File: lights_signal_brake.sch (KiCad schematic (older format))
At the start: 33 parts

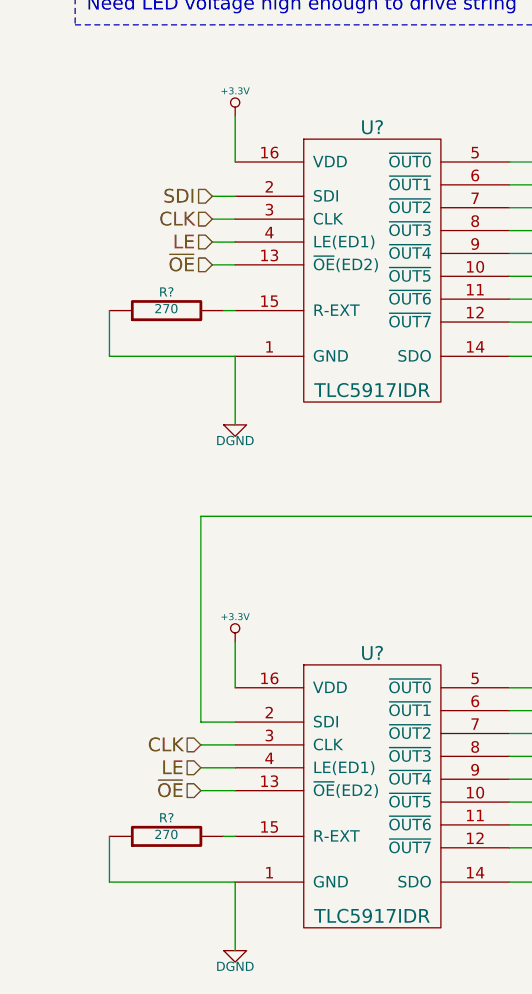
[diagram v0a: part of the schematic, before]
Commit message: Various components added
USB conn, general outputs, brake signal, touch sensor
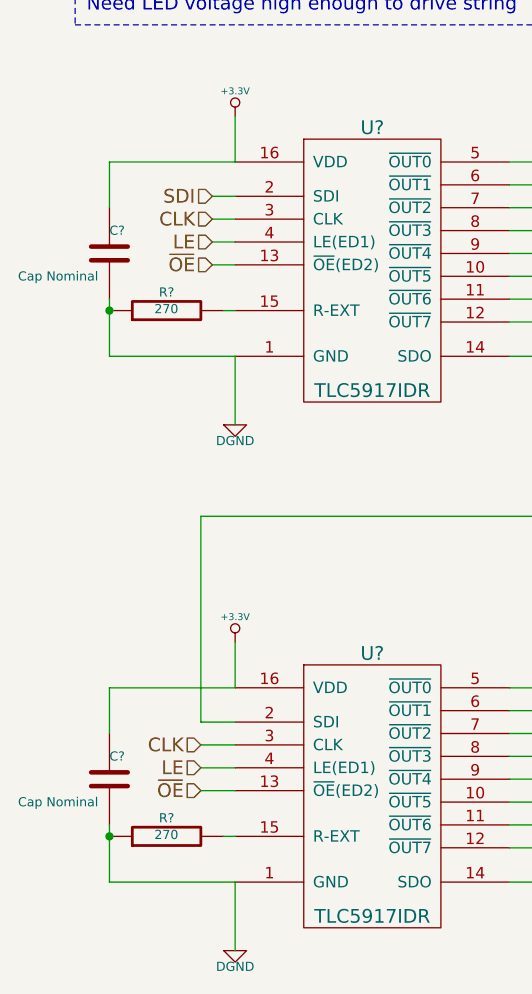
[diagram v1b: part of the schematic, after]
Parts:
- added C? (x2): Cap Nominal, ~, symbol C
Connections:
- net +3.3V: now also C?.1, C?.1
- net DGND: now also C?.2, C?.2
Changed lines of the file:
@@
 $Descr A4 11693 8268
 encoding utf-8
-Sheet 14 14
+Sheet 14 15
 Title ""
 Date "10 nov 2013"
@@
 	1550 4450 1600 4450
 Wire Wire Line
-	1050 4450 1050 4650
+	1050 4400 1050 4650
 Wire Wire Line
 	1050 4650 1600 4650
 Wire Wire Line
-	1050 2150 1050 2350
+	1050 2100 1050 2350
 Wire Wire Line
 	1050 2350 1600 2350
@@
 Text Notes 6000 1100 0    60   ~ 0
 Brake Signal
+$Comp
+L C C?
+U 1 1 527FF632
+P 1050 1900
+F 0 "C?" H 1050 2000 40  0000 L CNN
+F 1 "Cap Nominal" H 650 1800 40  0000 L CNN
+F 2 "~" H 1088 1750 30  0000 C CNN
+F 3 "~" H 1050 1900 60  0000 C CNN
+	1    1050 1900
+	1    0    0    -1
+$EndComp
+$Comp
+L C C?
+U 1 1 527FF638
+P 1050 4200
+F 0 "C?" H 1050 4300 40  0000 L CNN
+F 1 "Cap Nominal" H 650 4100 40  0000 L CNN
+F 2 "~" H 1088 4050 30  0000 C CNN
+F 3 "~" H 1050 4200 60  0000 C CNN
+	1    1050 4200
+	1    0    0    -1
+$EndComp
+Wire Wire Line
+	1050 1700 1050 1500
+Wire Wire Line
+	1050 1500 1600 1500
+Connection ~ 1050 2150
+Connection ~ 1050 4450
+Wire Wire Line
+	1050 4000 1050 3800
+Wire Wire Line
+	1050 3800 1600 3800
 $EndSCHEMATC
